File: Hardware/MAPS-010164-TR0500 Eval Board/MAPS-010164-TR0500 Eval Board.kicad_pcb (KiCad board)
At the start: 2 copper layers, 48.5 x 38.8 mm, 13 parts, among them IC1 MAPS-010164-TR0500, J1 Conn_Coaxial, J2 Conn_Coaxial, J3 Conn_02x02_Top_Bottom, J4 Conn_02x02_Top_Bottom, J5 Conn_02x04_Top_Bottom, J6 Conn_Coaxial, J7 Conn_Coaxial, J8 Conn_02x02_Top_Bottom

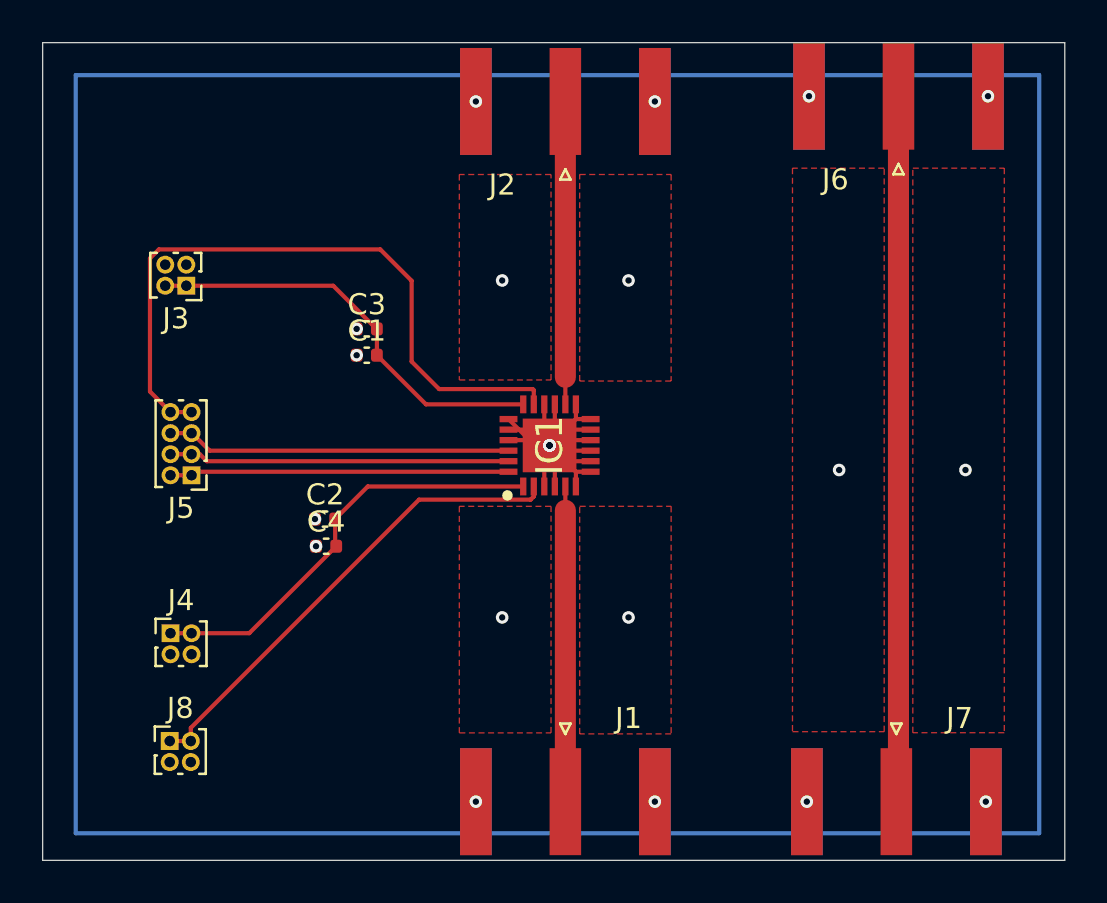
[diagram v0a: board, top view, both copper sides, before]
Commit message: Via stitching
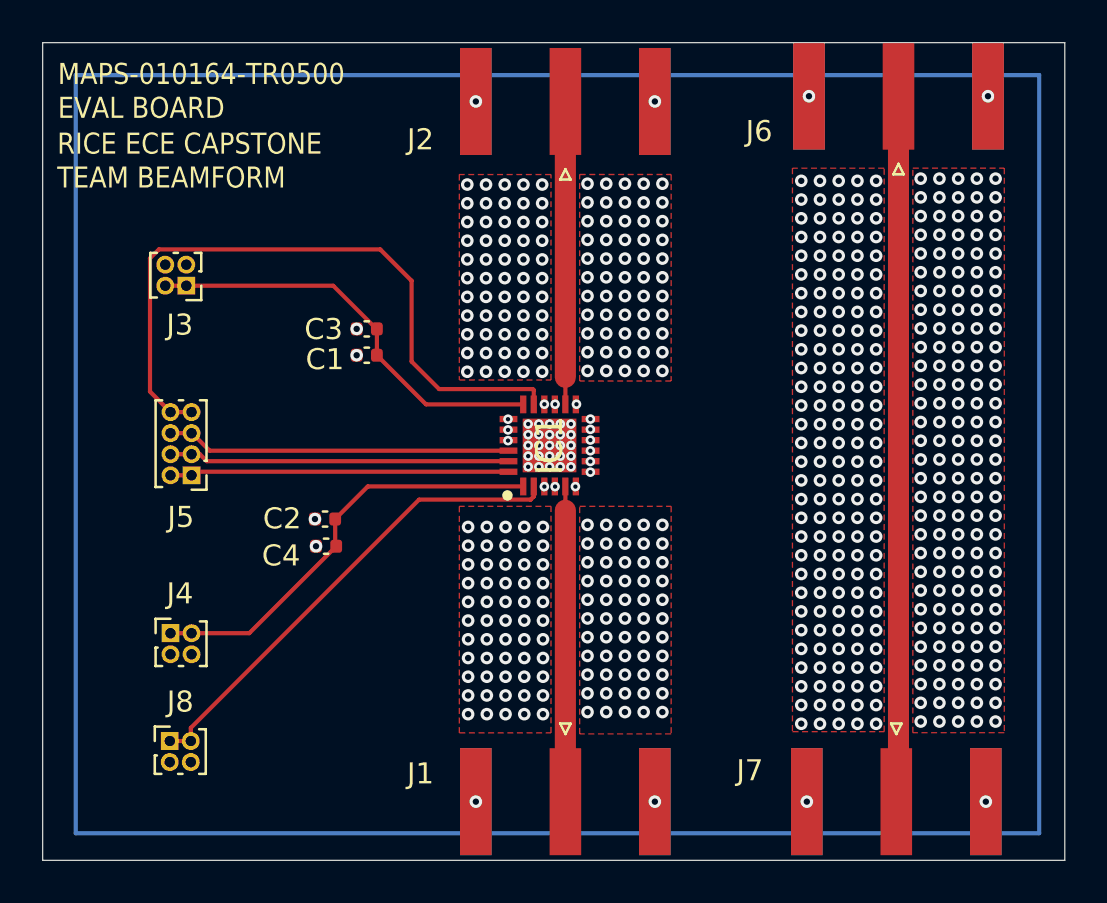
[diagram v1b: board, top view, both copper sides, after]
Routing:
- net GND: track 28.9 -> 1.42 mm, vias 21 -> 572
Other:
- board text added: "MAPS-010164-TR0500 EVAL BOARD"
- board text added: "RICE ECE CAPSTONE TEAM BEAMFORM"
